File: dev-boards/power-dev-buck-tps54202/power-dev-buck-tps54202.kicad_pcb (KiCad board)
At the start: 2 copper layers, 37 x 18 mm, 32 parts, among them J1 Conn_01x03, J2 Conn_01x03, J3 Conn_01x03, J4 Conn_01x03, J5 Screw_Terminal_01x02, J6 Screw_Terminal_01x02, SW1 SW_DIP_x04, U1 TPS54202DDCR

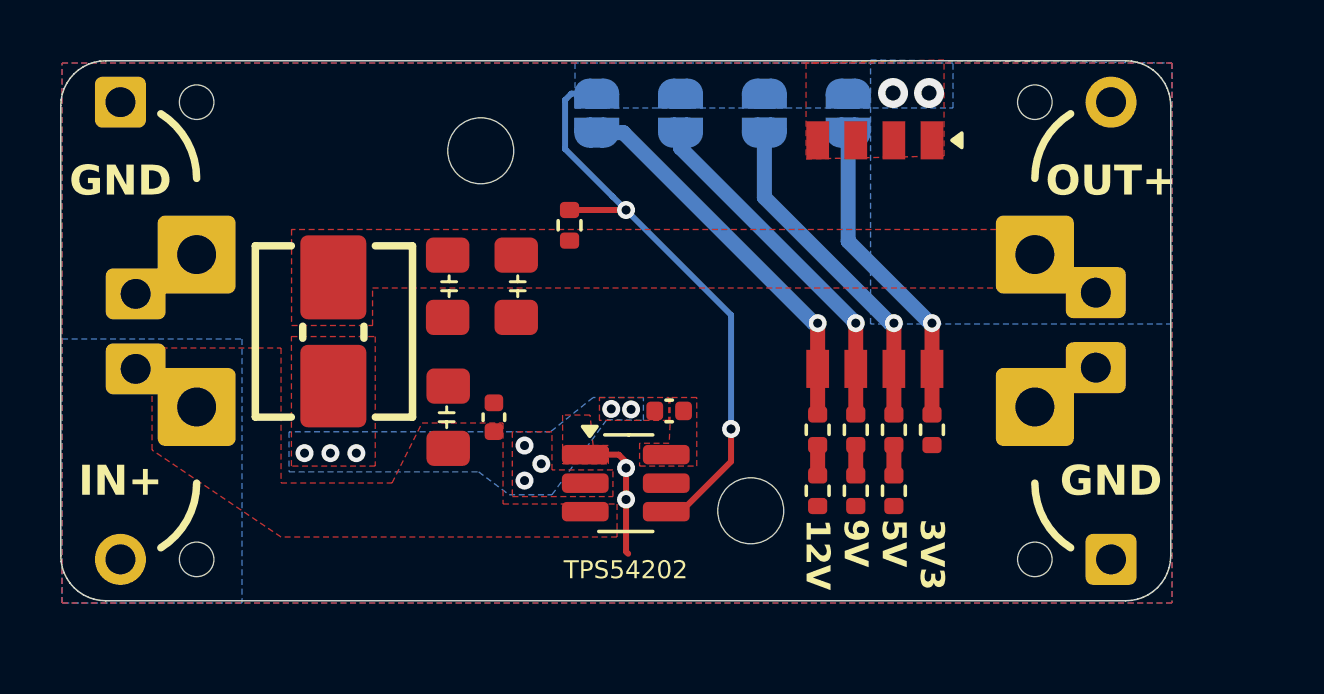
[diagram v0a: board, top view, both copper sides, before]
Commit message: Redesign power-dev-buck-tps54202
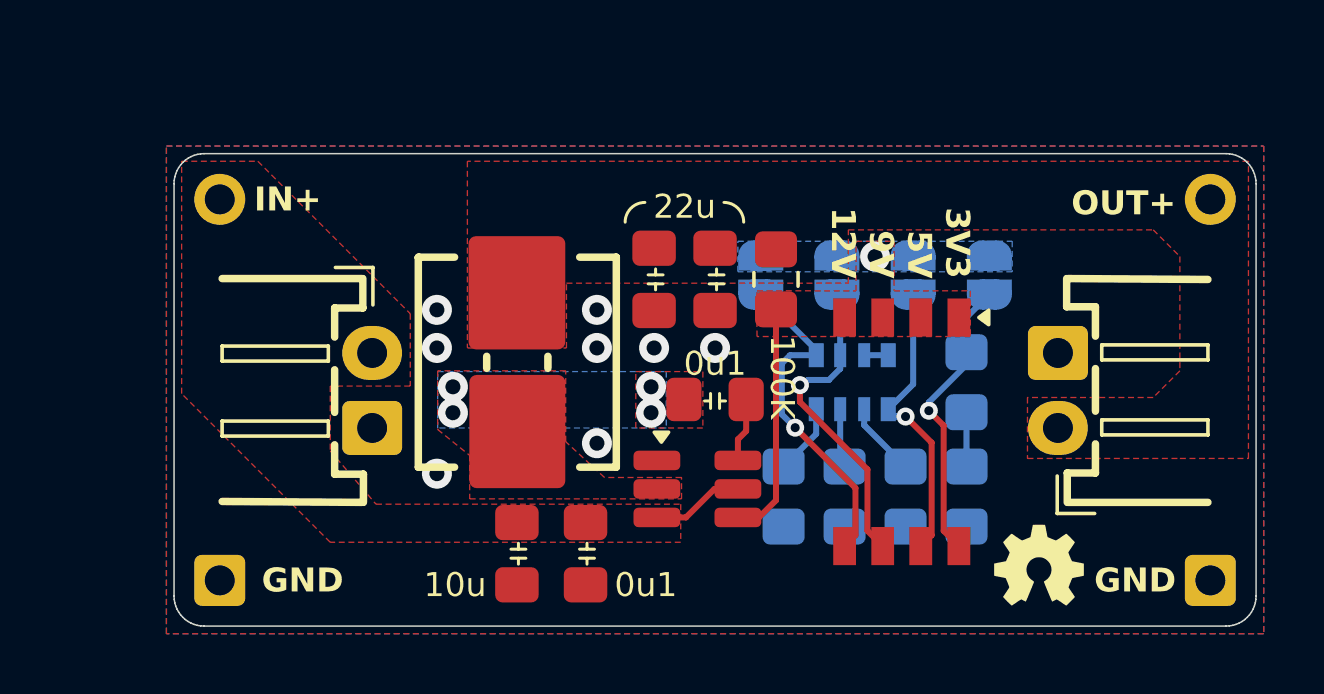
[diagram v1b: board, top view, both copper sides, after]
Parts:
- removed R3: 12K, Resistor_SMD:R_0402_1005Metric
- removed R5: 6.8K, Resistor_SMD:R_0402_1005Metric
- removed R7: 5.1K, Resistor_SMD:R_0402_1005Metric
- removed REF** (x4): jlcpcb-pcba-tooling-hole, custom:jlcpcb-pcba-tooling-hole
- removed REF** (x2): MountingHole_2.2mm_M2, MountingHole:MountingHole_2.2mm_M2
- added G***: LOGO, graphics:oshw-logo-3mm, F.Cu at (141.6, 146.8)
- added G***: LOGO, graphics:oshw-logo-3mm, B.Cu at (131.3, 140.7)
- added R0: 100K, Resistor_SMD:R_0805_2012Metric_Pad1.20x1.40mm_HandSolder, F.Cu at (132.8, 137.3)
- added RN1: 5K1, Resistor_SMD:R_Array_Convex_4x0603, B.Cu at (135.4, 140.7)
- C2, C3: footprint Capacitor_SMD:C_0402_1005Metric -> custom:C_0805_2012Metric_Pad1.18x1.45mm_HandSolder
- J5, J6: value Screw_Terminal_01x02 -> Conn_01x02; footprint custom:TerminalBlock_or_JST_2.54_1x02 -> custom:JST_XH_S2B-XH-2AW_1x02_P2.50mm_pad2gnd_trim2; moved to F.Cu
- L1: footprint custom:Inductor_Multi_5.2x5.7_2x2.5 -> custom:Inductor_Multi_7.0x6.6_plus
- R1: value 100K -> 10K; footprint Resistor_SMD:R_0402_1005Metric -> Resistor_SMD:R_0805_2012Metric_Pad1.20x1.40mm_HandSolder; moved to B.Cu
- R2: value 22K -> 12K; footprint Resistor_SMD:R_0402_1005Metric -> Resistor_SMD:R_0805_2012Metric_Pad1.20x1.40mm_HandSolder; moved to B.Cu
- R4: value 1K2 -> 3K; footprint Resistor_SMD:R_0402_1005Metric -> Resistor_SMD:R_0805_2012Metric_Pad1.20x1.40mm_HandSolder; moved to B.Cu
- R6: value 220R -> 1K8; footprint Resistor_SMD:R_0402_1005Metric -> Resistor_SMD:R_0805_2012Metric_Pad1.20x1.40mm_HandSolder; moved to B.Cu
- R8: value 120R -> 100R; footprint Resistor_SMD:R_0402_1005Metric -> Resistor_SMD:R_0805_2012Metric_Pad1.20x1.40mm_HandSolder; moved to B.Cu
- U1: footprint Package_TO_SOT_SMD:SOT-23-6_Handsoldering -> custom:SOT-23-6_Handsoldering_simple
- moved J4 16.3 mm to (114.3, 147.3)
- moved R1 16.0 mm to (139.2, 144.5), turned to -90 degrees
- moved J1 12.4 mm to (114.3, 134.6)
- moved JP4 7.68 mm to (132.3, 137.1)
- moved JP3 7.51 mm to (134.9, 137.1)
- moved JP2 7.33 mm to (137.4, 137.1)
- moved JP1 7.16 mm to (140.0, 137.1)
- moved C4 6.89 mm to (128.8, 137.3)
- moved C5 6.63 mm to (130.8, 137.3)
- moved L1 6.22 mm to (124.2, 140.0)
- moved SW1 5.97 mm to (137.0, 142.4)
- moved J5 5.88 mm to (119.4, 141.0), turned to -90 degrees
- moved C2 5.48 mm to (126.5, 146.4), turned to -90 degrees
- moved C1 5.09 mm to (124.2, 146.4), turned to -90 degrees
- moved J3 4.63 mm to (147.3, 134.6)
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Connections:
- R1 pad 1: VOUT -> Net-(R1-Pad1)
- R1 pad 2: FB -> GND
- R2 pad 2: GND -> Net-(R1-Pad1)
- U1 pad 5: unconnected-(U1-EN-Pad5) -> VIN
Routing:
- net FB: track 20.2 -> 7.87 mm, vias 4 -> 1
- net GND: track 4.55 -> 0.00 mm, vias 2 -> 8
- net VIN: track 0.00 -> 3.09 mm
- net BOOT: track 0.00 -> 2.15 mm
- net Net-(R1-Pad1): track 0.00 -> 1.81 mm
- net 12V_SELECT: track 13.0 -> 11.3 mm
- net 5V_SELECT: track 11.3 -> 9.67 mm
- net Net-(RN1C-R3.2): track 1.01 -> 2.48 mm
- net Net-(RN1A-R1.2): track 1.01 -> 2.36 mm
- net 9V_SELECT: track 11.8 -> 10.6 mm
- net Net-(RN1B-R2.2): track 1.01 -> 1.97 mm
- net 3V3_SELECT: track 10.6 -> 9.63 mm
- net Net-(RN1C-R3.1): track 0.00 -> 0.80 mm
- net VOUT: track 0.00 -> 0.59 mm
- net SW: track 0.00 -> 0.22 mm, vias 8 -> 4
- removed copper zone on F.Cu, net BOOT
- removed copper zone on B.Cu, net VIN
- removed copper zone on B.Cu, net VOUT
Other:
- board size 37 x 18 mm -> 36.1 x 15.7 mm
- board text added: "0u1"
- board text added: "100K"
- board text added: "100R"
- board text added: "10K"
- board text added: "10u"
- board text added: "12K"
- board text added: "1K8"
- board text added: "22u"
- board text added: "3K"
- board text added: "5K1"
- board text added: "8-24V buck converter TPS54202"
- board text added: "github.com/smkent/pcb 2024"
- board text removed: "DC-DC buck / In: 4.5-28V"
- board text removed: "Power Dev"
- board text removed: "TPS54202"

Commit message: Add power indicator LED
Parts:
- added D1: LED, custom:LED_0805_2012Metric_Pad1.15x1.40mm_HandSolder_simple, F.Cu at (132.5, 147.1)
- added R10: 1K, Resistor_SMD:R_0805_2012Metric_Pad1.20x1.40mm_HandSolder, F.Cu at (141.6, 147.1)
- moved G*** 11.4 mm to (141.1, 135.4)
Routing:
- net GND: track 0.00 -> 19.9 mm, vias 8 -> 10
- net Net-(D1-A): track 0.00 -> 7.17 mm
- net VOUT: track 0.59 -> 5.57 mm
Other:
- board text added: "8-24V buck converter TPS54202DDCR"
- board text removed: "8-24V buck converter TPS54202"
